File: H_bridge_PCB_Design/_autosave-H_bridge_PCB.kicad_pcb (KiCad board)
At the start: 2 copper layers, 110.2 x 110.2 mm, 128 parts, among them IC1 LM2671M-3.3_NOPB, IC2 L7812ABD2T-TR, IC5 ACS37800KMACTR-030B3-I2C, J1 TSW-102-15-T-S, J12 TSW-102-15-T-S, J13 1734510-1, J14 TSW-102-15-T-S, J15 TSW-102-15-T-S, J2 TSW-102-15-T-S, J3 TSW-102-15-T-S, J4 TSW-102-15-T-S, J5 TSW-102-15-T-S, J7 TSW-102-15-T-S, J9 TSW-102-15-T-S, Q1 IRLB4030PBF, Q10 IPD90N10S4L06ATMA1, Q11 NTR2101P, Q12 NTR2101P, Q2 IRLB4030PBF, Q3 IRLB4030PBF, Q4 IRLB4030PBF, Q5 IPD90N10S4L06ATMA1, Q6 IPD90N10S4L06ATMA1, Q7 BC817, Q8 BC817, Q9 IPD90N10S4L06ATMA1, U1 ESP32-WROOM-32, U2 IR2110S, U3 IR2110S, U4 INA228, U5 LTC4412xS6, U6 LD1086DT50TR, U7 CH340C, U8 3544-2, U9 LT1963AxST-3.3

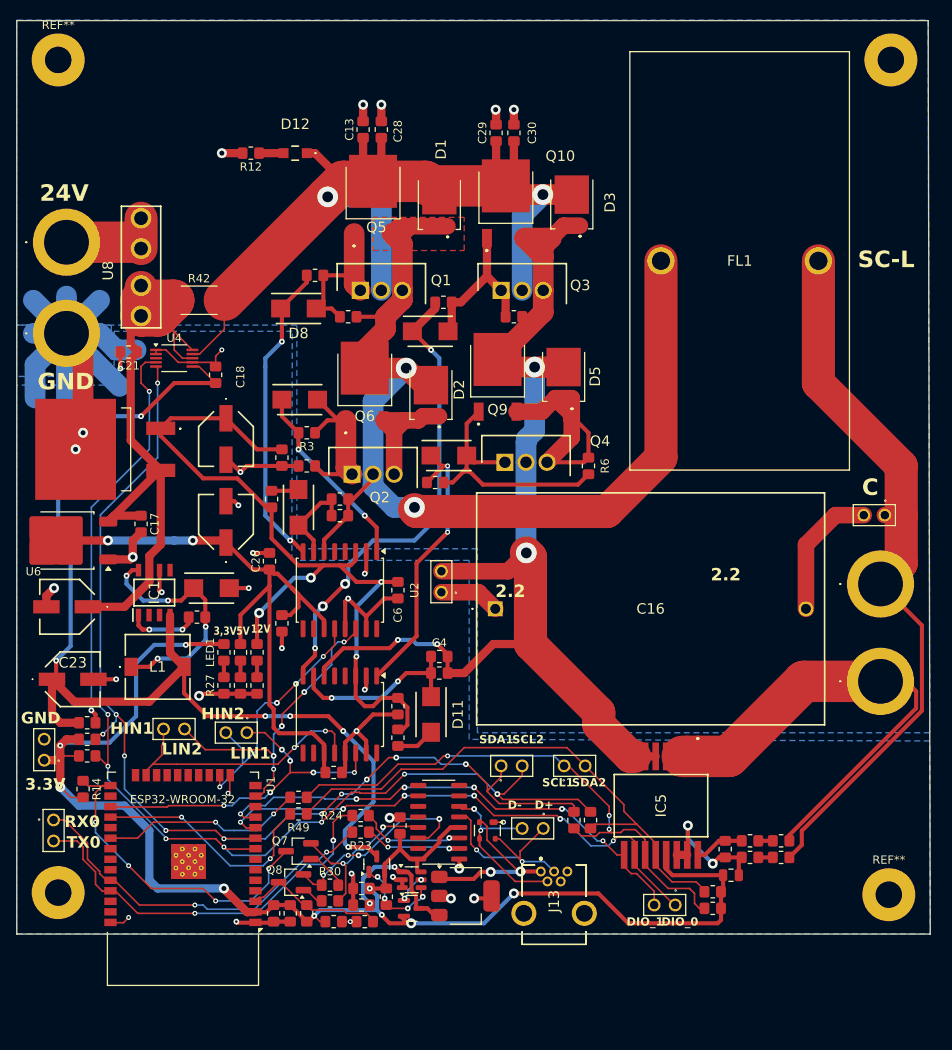
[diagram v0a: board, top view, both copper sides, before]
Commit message: -Changed PCB Layout now with 2x 3.3V also from usb, and to different ground planes -Measurement output now correctly parametrized -Stop sequence changed for SC protection
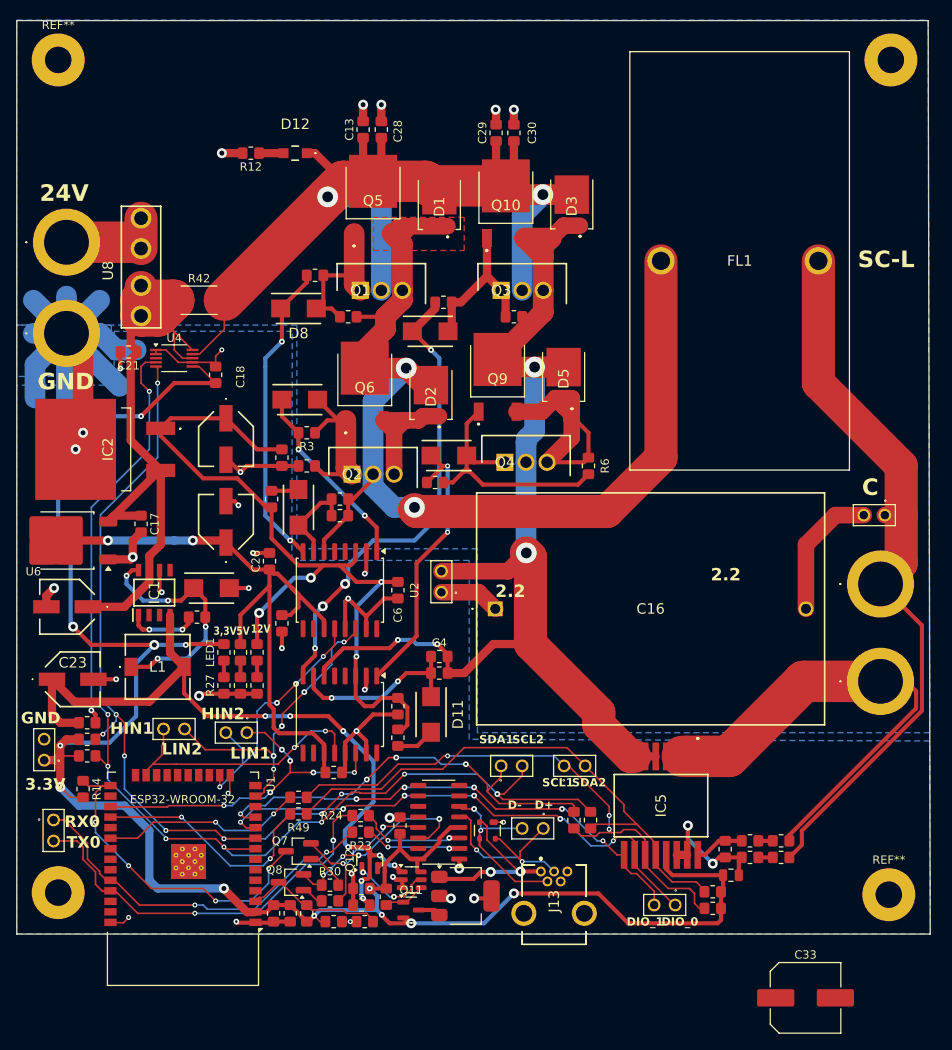
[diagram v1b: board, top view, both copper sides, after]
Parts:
- added C33: 1.5mF, Capacitor_SMD:C_Elec_8x10.2, F.Cu at (145.2, 157.2)
- moved Q12 0.97 mm to (92.6, 140.6)
- moved Q11 0.21 mm to (97.6, 146.6)
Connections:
- C18 pad 1: VIN(3.3V) -> +3.3V
- C31 pad 1: VUSB(3.3V) -> VIN(3.3V)
- R11 pad 2: Net-(Q12-G) -> Net-(Q11-G)
- U4 pad 6: VIN(3.3V) -> +3.3V
- U5 pad 1: VUSB(3.3V) -> VIN(3.3V)
- U5 pad 4: Net-(Q12-G) -> Net-(Q11-G)
- U5 pad 5: Net-(Q11-G) -> Net-(Q12-G)
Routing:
- net +3.3V: track 180.8 -> 242.8 mm, vias 9 -> 12
- net VIN(3.3V): track 136.0 -> 92.0 mm, vias 6 -> 8
- net VUSB(3.3V): track 17.9 -> 2.71 mm, vias 2 -> 0
- net Net-(Q11-G): track 3.86 -> 5.92 mm, vias 2 -> 0
- net Net-(Q12-G): track 11.5 -> 9.96 mm, vias 4 -> 2
